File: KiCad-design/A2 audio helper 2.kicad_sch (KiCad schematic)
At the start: 30 parts

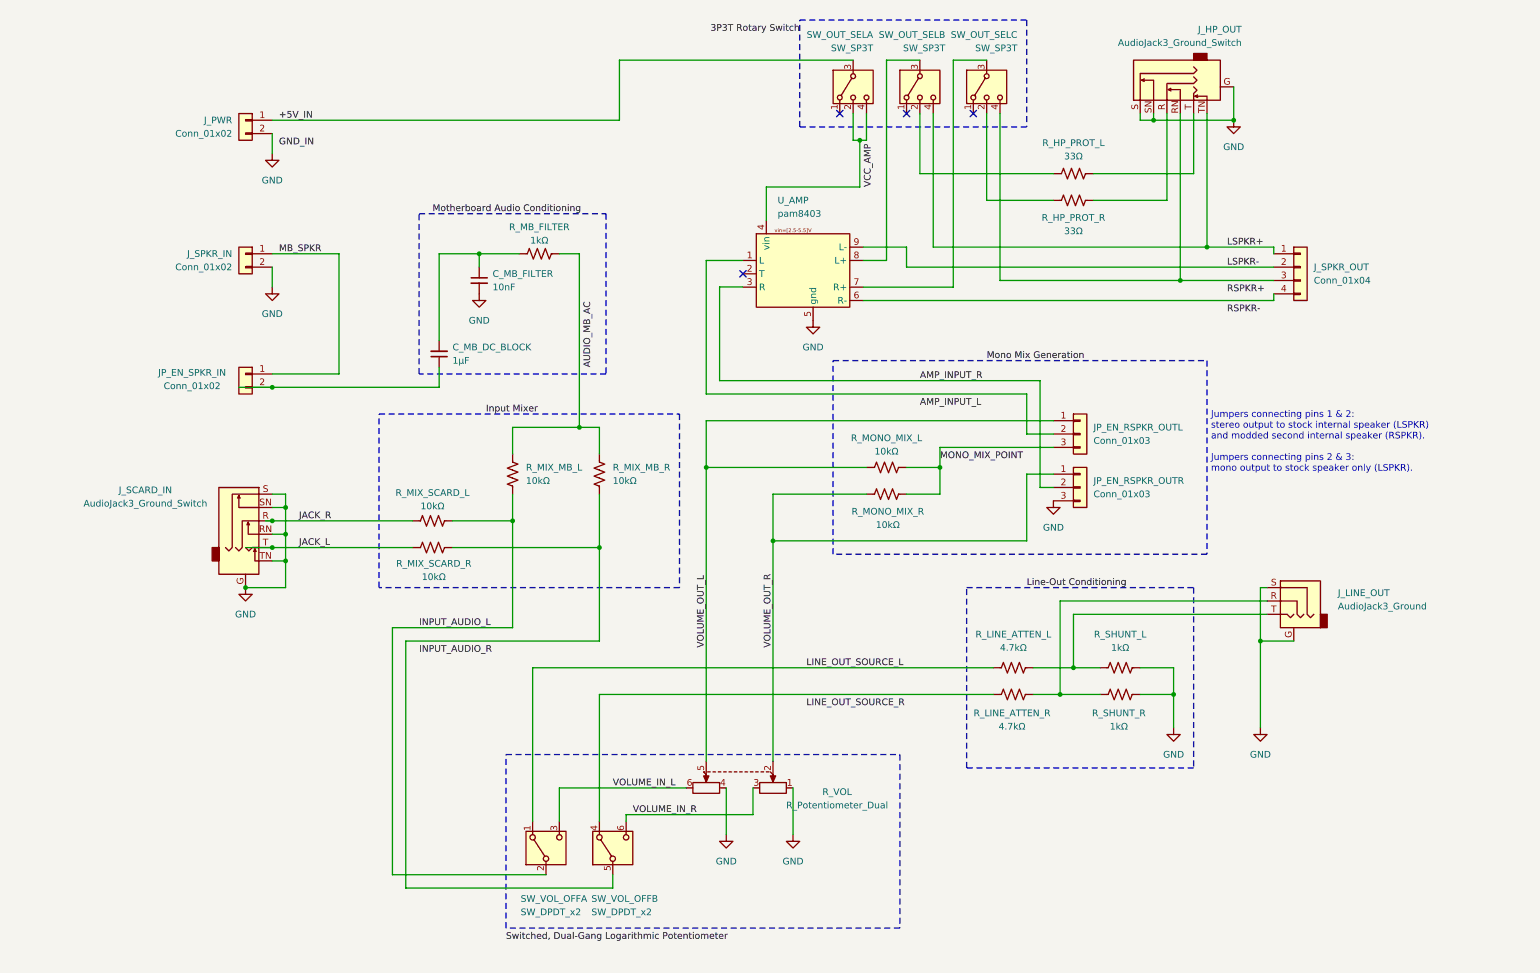
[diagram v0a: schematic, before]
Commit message: add guide textfile, revise sc. for simulation WIP
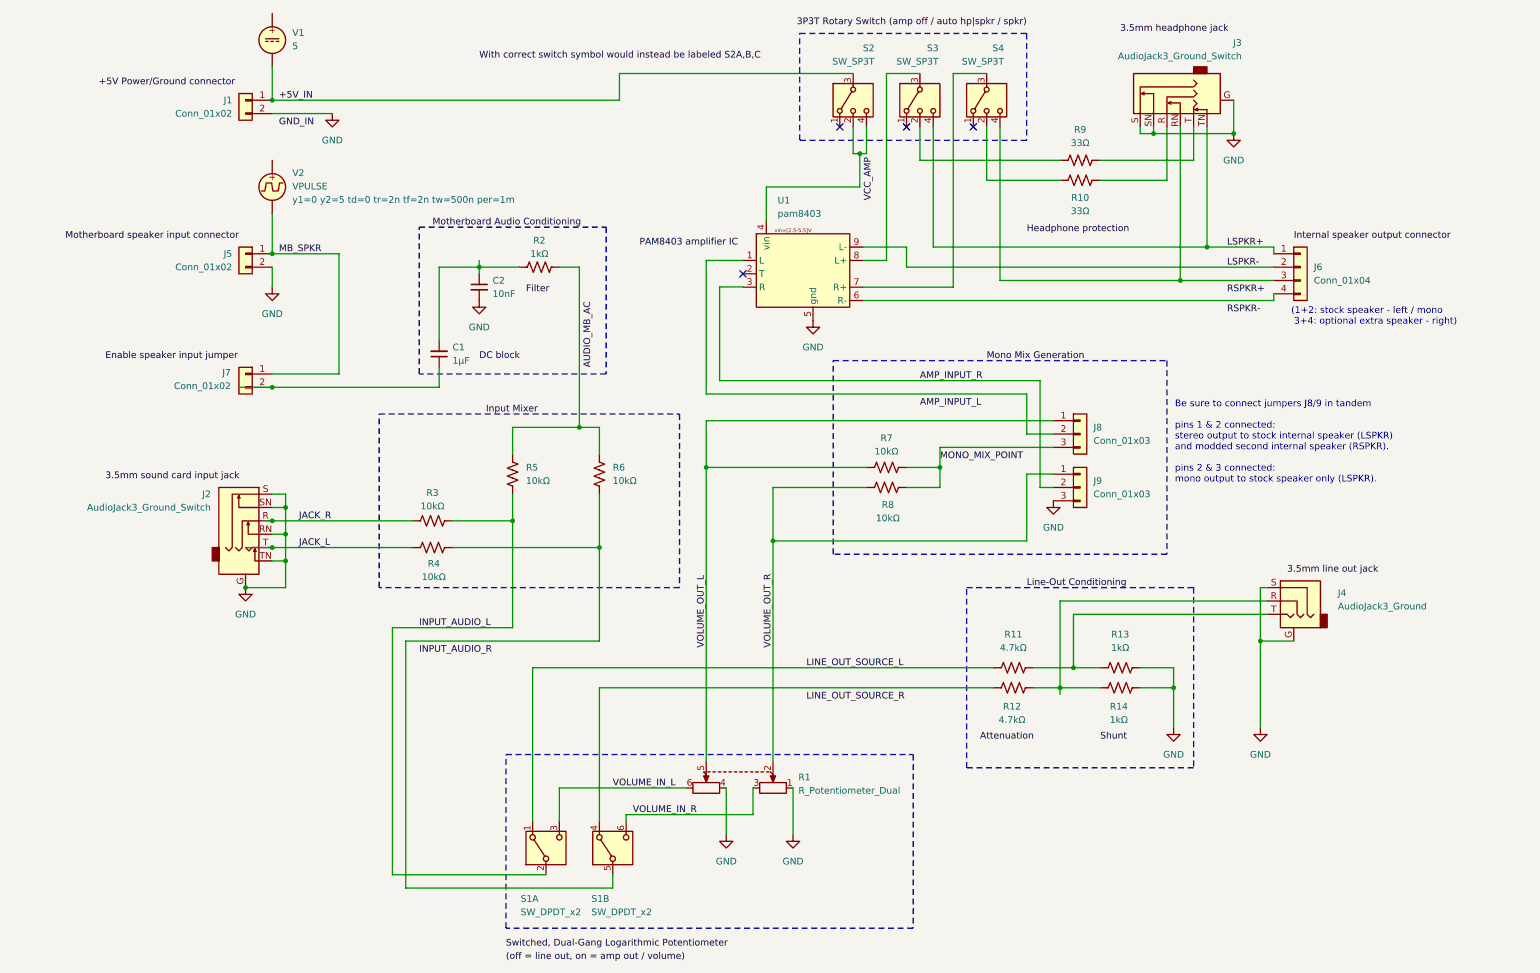
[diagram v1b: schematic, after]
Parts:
- added V1: 5, symbol Simulation_SPICE:VDC
- added V2: VPULSE, symbol Simulation_SPICE:VPULSE
- renumbered C_MB_DC_BLOCK to C1, C_MB_FILTER to C2, J_PWR to J1, J_SCARD_IN to J2, J_HP_OUT to J3, J_LINE_OUT to J4, J_SPKR_IN to J5, J_SPKR_OUT to J6, JP_EN_SPKR_IN to J7, JP_EN_RSPKR_OUTL to J8, JP_EN_RSPKR_OUTR to J9, R_VOL to R1, R_HP_PROT_R to R10, R_LINE_ATTEN_L to R11, R_LINE_ATTEN_R to R12, R_SHUNT_L to R13, R_SHUNT_R to R14, R_MB_FILTER to R2, R_MIX_SCARD_L to R3, R_MIX_SCARD_R to R4, R_MIX_MB_L to R5, R_MIX_MB_R to R6, R_MONO_MIX_L to R7, R_MONO_MIX_R to R8, R_HP_PROT_L to R9, SW_VOL_OFF to S1, SW_OUT_SELA to S2, SW_OUT_SELB to S3, SW_OUT_SELC to S4, U_AMP to U1
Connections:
- net +5V_IN: now also V1.2
- net MB_SPKR: now also V2.2
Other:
- note added: "(1+2: stock speaker - left / mono 3+4: optional extra speaker - right)"
- note added: "Be sure to connect jumpers J8/9 in tandem pins 1 & 2 connected: stereo output to stock internal speaker (LSPKR) and modded second internal speaker (RSPKR). pins 2 & 3 connected: mono output to stock speaker only (LSPKR)."
- note removed: "Jumpers connecting pins 1 & 2: stereo output to stock internal speaker (LSPKR) and modded second internal speaker (RSPKR). Jumpers connecting pins 2 & 3: mono output to stock speaker only (LSPKR)."
- moved on the sheet: C2, J1, J3, R10, R12, R14, R2, R8, R9, S2, S3, S4

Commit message: revision 4 of the guide & schematic
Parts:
- removed R1: R_Potentiometer_Dual, symbol Device:R_Potentiometer_Dual
- removed S1: SW_DPDT_x2, symbol Switch:SW_DPDT_x2
- removed S2, S3, S4: SW_SP3T, symbol Switch:SW_SP3T
- removed V1: 5, symbol Simulation_SPICE:VDC
- removed V2: VPULSE, symbol Simulation_SPICE:VPULSE
- added D1: D_Small, symbol Device:D_Small
- added J10: 0.05, symbol Connector_Generic:Conn_01x02
- added K1: Relay_DPDT, symbol Relay:Relay_DPDT
- added R1: PTR902-1020K-A502, PTR902-1020K-A502:TRIM_PTR902-1020K-A502, symbol PTR902-1020K-A502:PTR902-1020K-A502
- added SW2: SW_DPDT_x2, symbol Switch:SW_DPDT_x2
- J1: value Conn_01x02 -> 5
- J7: value Conn_01x02 -> 0.05
- renumbered R4 to R3, R3 to R4, R6 to R5, R5 to R6
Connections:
- net JACK_L is gone; now on net GND: J2.T, R3.1
- net JACK_R is gone; now on net GND: J2.R, R4.1
- net VOLUME_OUT_R is gone; now on net VOLUME_OUT_L: J9.1 (Pin_1), R8.1
- net +5V_IN: now also J10.1 (Pin_1)
- net AMP_INPUT_L: now also J8.2 (Pin_2)
- net GND: now also D1.2 (A), K1.A2
- net INPUT_AUDIO_L: now also R3.2, R5.2, K1.11; no longer R4.2, R6.2
- net INPUT_AUDIO_R: now also R4.2, R6.2, K1.21
- net LINE_OUT_SOURCE_L: now also K1.12
- net LSPKR+: now also SW2.1 (A)
- net RSPKR+: now also J3.RN, J6.3 (Pin_3), SW2.4 (A)
- net RSPKR-: now also J6.4 (Pin_4), U1.6 (R-)
- net VOLUME_IN_L: now also K1.14, R1.R1_1
- net VOLUME_IN_R: now also K1.24, R1.R2_1
- net VOLUME_OUT_L: now also R1.R1_3, R1.R2_3
- net at J4.R, R12.1, R14.1: now also J4.T, R11.2, R13.1
- net at R12.2: now also K1.22
- net at R10.1: now also SW2.6 (C)
- net at U1.7 (R+): now also SW2.5 (B)
- net at R9.1: now also SW2.3 (C)
- net at U1.8 (L+): now also SW2.2 (B)
- net AMP_CONTROL: now reaches U1.4 (vin)
- net AMP_CONTROL: now also D1.1 (K), K1.A1, R1.NO
- new net SWITCHED_V_IN: J10.2 (Pin_2), R1.COM
- no-connect marks 4 -> 1
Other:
- note added: "1+2: stock speaker - left / mono 3+4: optional extra speaker - right"
- note added: "Jumpers J8/9 are to be connected in tandem pins 1 & 2 connected: stereo output to stock internal speaker (LSPKR) and modded second internal speaker (RSPKR). pins 2 & 3 connected: mono output to stock speaker only (LSPKR)."
- note added: "PAM8403 amplifier IC"
- note added: "off = Amplifier off, Audio Input directed to Line-Out on = Audio Input to Potentiometer enabled, Amplifier on, Volume output from Potentiometer sent to Amplifier (via Mono Mixer), Line-Out disabled"
- note removed: "(1+2: stock speaker - left / mono 3+4: optional extra speaker - right)"
- note removed: "Be sure to connect jumpers J8/9 in tandem pins 1 & 2 connected: stereo output to stock internal speaker (LSPKR) and modded second internal speaker (RSPKR). pins 2 & 3 connected: mono output to stock speaker only (LSPKR)."
- moved on the sheet: C1, C2, J1, J2, J3, J5, J7, J8, J9, R10, R11, R12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

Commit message: fixed schematic mistakes & warnings
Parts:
- D1: value D_Small -> 1N4148
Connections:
- net AMP_INPUT_L: now also U1.1 (L)
- net AMP_INPUT_R: now also U1.3 (R)
- net AUDIO_MB_AC: now also R2.2, R5.1, R6.1
- net GND: now also R1.R1_3, R1.R2_3; no longer J2.R, J2.T, R3.1, R4.1
- net LINE_OUT_SOURCE_R: now also K1.22, R12.2
- net VOLUME_OUT_L: now also R1.R1_2; no longer R1.R1_3, R1.R2_3, R8.1
- net VOLUME_OUT_R: now reaches R1.R2_2
- net VOLUME_OUT_R: now also R8.1
- new net JACK_L: J2.T, R3.1
- new net JACK_R: J2.R, R4.1
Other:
- note added: "+5V Power/Ground connector"
- note added: "10KΩ Dual-gang logarithmic potentiometer, switched"
- note added: "3.5mm headphone jack"
- note added: "3.5mm line-out jack"
- note added: "3.5mm sound card input jack"
- note added: "Amplifier module"
- note added: "Attenuation"
- note added: "DC block"
- note added: "Enable amplifier jumper"
- note added: "Enable speaker input jumper"
- note added: "Filter"
- note added: "Flyback diode"
- note added: "Headphone protection"
- note added: "Input Mixer"
- note added: "Internal speaker output connector"
- note added: "Line-Out Conditioning"
- note added: "Mode Selection, Power & Audio Routing"
- note added: "Mono Mix Generation"
- note added: "Motherboard Audio Conditioning"
- note added: "Motherboard speaker input connector"
- note added: "Shunt"
- note removed: "PAM8403 amplifier IC"

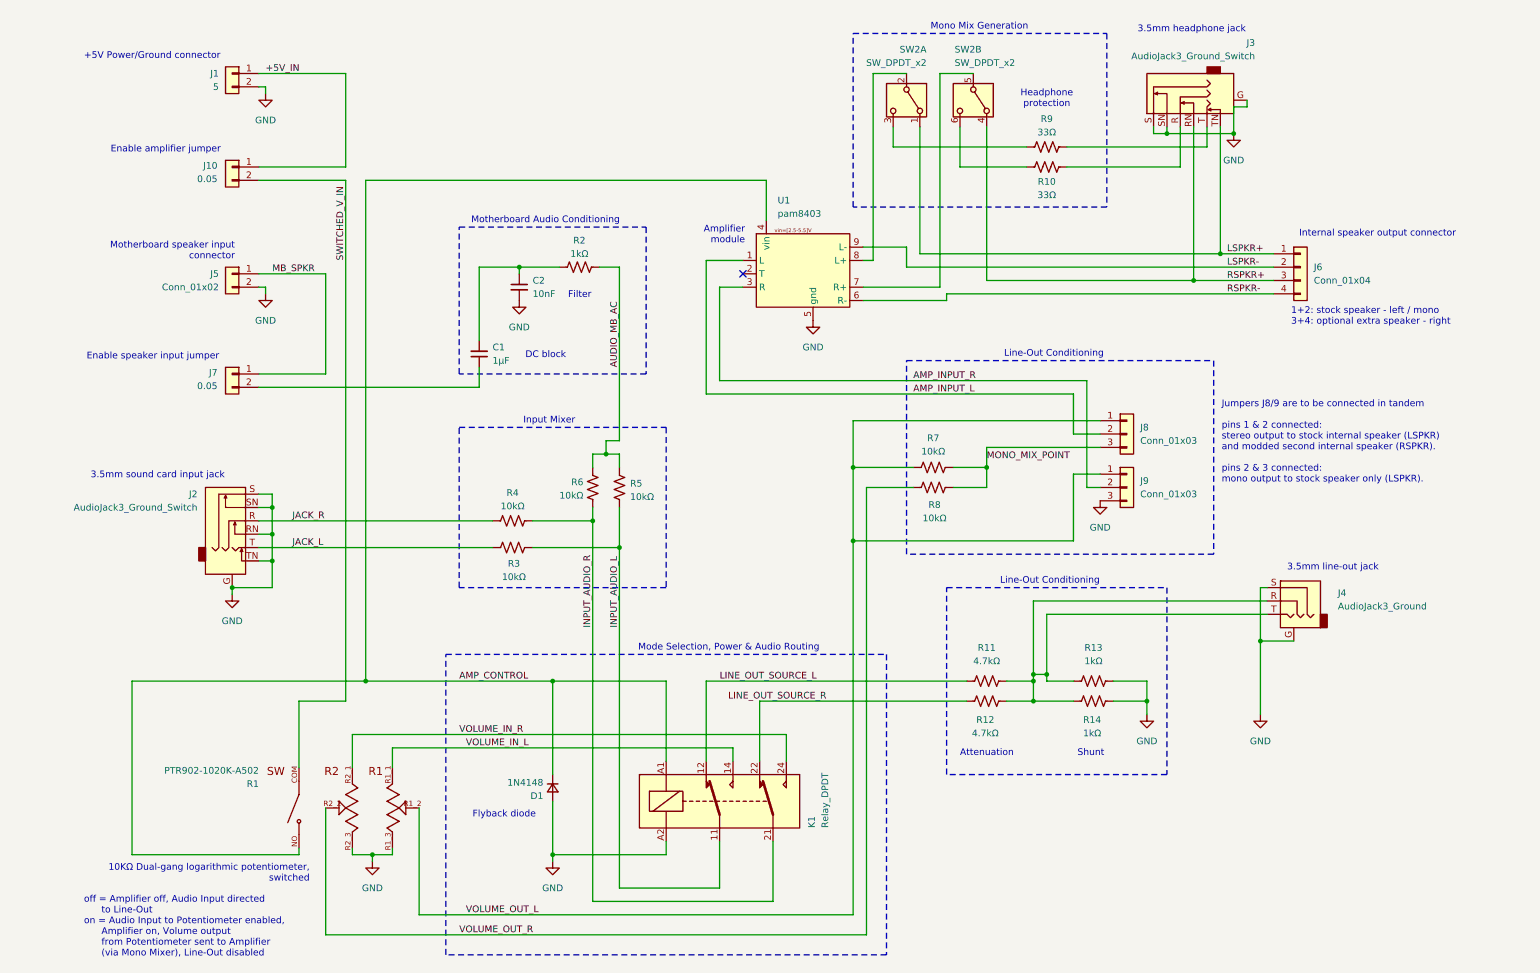
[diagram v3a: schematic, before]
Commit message: fixed schematic issues from sim attempts, better layout
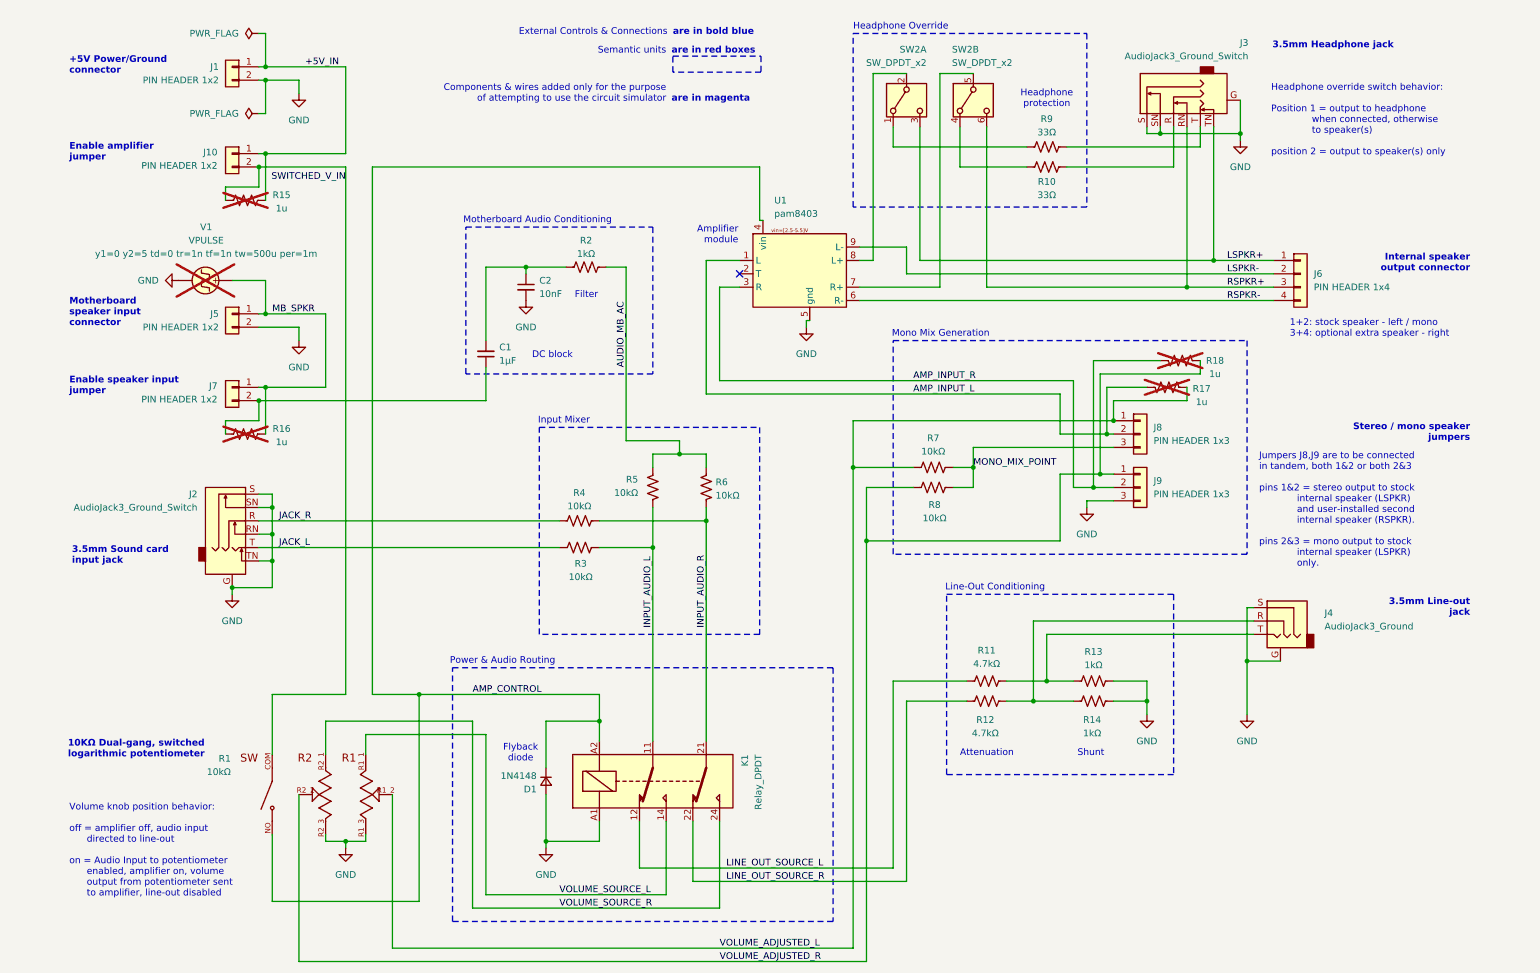
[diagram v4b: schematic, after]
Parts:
- added R15, R16, R17, R18: 1u, symbol Device:R_US
- added V1: VPULSE, symbol Simulation_SPICE:VPULSE
- J1: value 5 -> PIN HEADER 1x2
- J10, J7: value 0.05 -> PIN HEADER 1x2
- J5: value Conn_01x02 -> PIN HEADER 1x2
- J6: value Conn_01x04 -> PIN HEADER 1x4
- J8, J9: value Conn_01x03 -> PIN HEADER 1x3
- R1: value PTR902-1020K-A502 -> 10kΩ
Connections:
- net +5V_IN: now also R15.2
- net AMP_CONTROL: now also K1.A2; no longer K1.A1
- net AMP_INPUT_L: now also R17.2
- net AMP_INPUT_R: now also R18.2
- net GND: now also K1.A1, V1.2; no longer K1.A2
- net LSPKR+: now also SW2.3 (C); no longer SW2.1 (A)
- net MB_SPKR: now also R16.2, V1.1
- net RSPKR+: now also SW2.6 (C); no longer SW2.4 (A)
- net SWITCHED_V_IN: now also R15.1
- net at J4.R, R12.1, R14.1: no longer J4.T, R11.2, R13.1
- net at C1.1, J7.2 (Pin_2): now also R16.1
- net at R10.1: now also SW2.4 (A); no longer SW2.6 (C)
- net at R9.1: now also SW2.1 (A); no longer SW2.3 (C)
- net VOLUME_IN_L renamed VOLUME_SOURCE_L
- net VOLUME_IN_R renamed VOLUME_SOURCE_R
- net VOLUME_OUT_L renamed VOLUME_ADJUSTED_L
- net VOLUME_ADJUSTED_L: now also R17.1; no longer J9.1 (Pin_1)
- net VOLUME_OUT_R renamed VOLUME_ADJUSTED_R
- net VOLUME_ADJUSTED_R: now also J9.1 (Pin_1), R18.1
- new net: J4.T, R11.2, R13.1
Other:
- note added: "10KΩ Dual-gang, switched logarithmic potentiometer"
- note added: "3.5mm Headphone jack"
- note added: "3.5mm Line-out jack"
- note added: "3.5mm Sound card input jack"
- note added: "Components & wires added only for the purpose of attempting to use the circuit simulator"
- note added: "External Controls & Connections"
- note added: "Headphone Override"
- note added: "Headphone override switch behavior: Position 1 = output to headphone when connected, otherwise to speaker(s) position 2 = output to speaker(s) only"
- note added: "Jumpers J8,J9 are to be connected in tandem, both 1&2 or both 2&3 pins 1&2 = stereo output to stock internal speaker (LSPKR) and user-installed second internal speaker (RSPKR). pins 2&3 = mono output to stock internal speaker (LSPKR) only."
- note added: "Power & Audio Routing"
- note added: "Semantic units"
- note added: "Stereo / mono speaker jumpers"
- note added: "Volume knob position behavior: off = amplifier off, audio input directed to line-out on = Audio Input to potentiometer enabled, amplifier on, volume output from potentiometer sent to amplifier, line-out disabled"
- note added: "are in bold blue"
- note added: "are in magenta"
- note added: "are in red boxes"
- note removed: "10KΩ Dual-gang logarithmic potentiometer, switched"
- note removed: "3.5mm headphone jack"
- note removed: "3.5mm line-out jack"
- note removed: "3.5mm sound card input jack"
- note removed: "Jumpers J8/9 are to be connected in tandem pins 1 & 2 connected: stereo output to stock internal speaker (LSPKR) and modded second internal speaker (RSPKR). pins 2 & 3 connected: mono output to stock speaker only (LSPKR)."
- note removed: "Mode Selection, Power & Audio Routing"
- note removed: "off = Amplifier off, Audio Input directed to Line-Out on = Audio Input to Potentiometer enabled, Amplifier on, Volume output from Potentiometer sent to Amplifier (via Mono Mixer), Line-Out disabled"
- moved on the sheet: C1, C2, D1, J1, J10, J3, J4, J5, J6, J7, J8, J9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
